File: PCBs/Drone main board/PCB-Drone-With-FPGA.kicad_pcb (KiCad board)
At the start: 4 copper layers, 60 x 100 mm, 213 parts, among them J1001 Conn_02x10, J1002 Conn_02x07, J1003 Conn_02x10, J1004 Conn_02x05, J201 PJ-102A, J601 UJ2-MBH-1-SMT-TR, J801 SMA-RP, J901 Amphenol-1mm-10-header, U1201 10CL040_F484, U301 AP63205WU-7, U401 SC189ZSKTRT, U402 NCP115ASN250T2G, U501 AP63200WU-7, U601 93LCxxBxxOT, U602 FT232H, U603 MT25QL512ABB8ESF-0SIT, U604 W25Q128JVS, U701 ICM-20602, U702 TXB0108PWR, U703 BNO055, U704 DPS422XTSA1, U705 MCP3208, U801 nRF24L01P, U802 RFX2401C, X1401 SiT2001B1-S2-33E-50, X801 16MHz, Y601 12MHz, Y701 32.7KHz

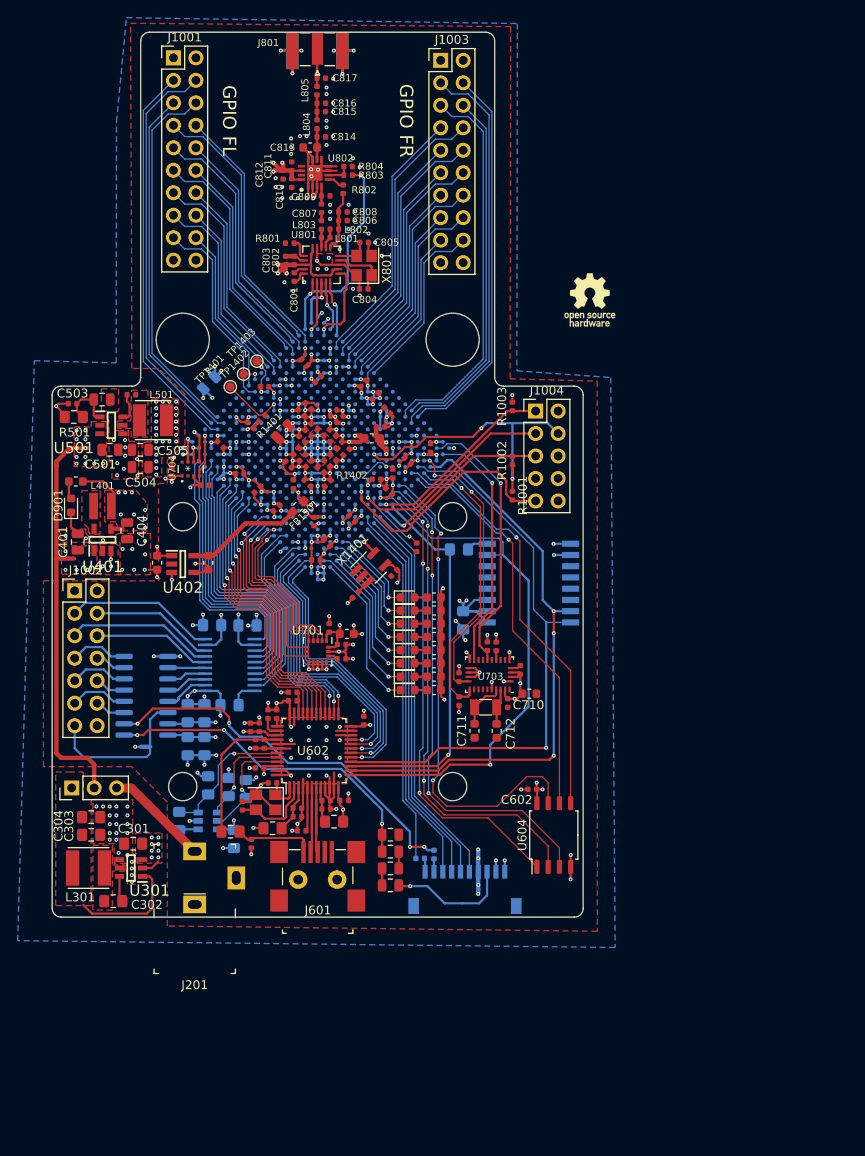
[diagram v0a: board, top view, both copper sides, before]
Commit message: Redid the radio PCB layout on both drone and remote PCB. Drone PCB had old schematic, remote PCB layout wasn't ideal.
Copied in the VHDL project files from the seperate VHDL project into the main "All in one" project.

Signed-off-by: Eldalote.Electronics <Eldalote.Electronics@gmail.com>
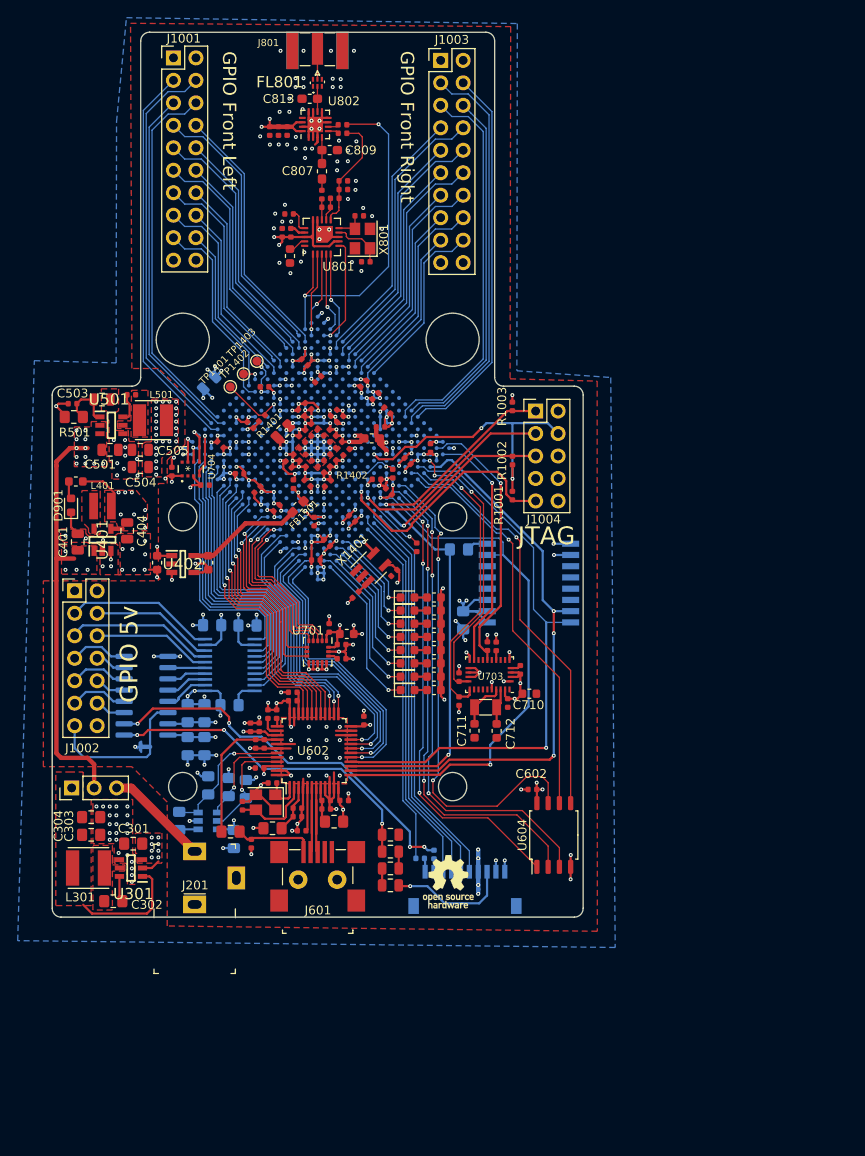
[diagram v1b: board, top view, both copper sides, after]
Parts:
- removed C814, C815, C816, C817: 1pF, Capacitor_SMD:C_0402_1005Metric
- removed L804, L805: 2.7nH, Inductor_SMD:L_0402_1005Metric
- removed R804: 2K, Resistor_SMD:R_0402_1005Metric
- added FL801: 2450LP14A100T, SamacSys_Parts:2450LP14A100T, F.Cu at (130.0, 45.7)
- C801: footprint Capacitor_SMD:C_0402_1005Metric -> Capacitor_SMD:C_0603_1608Metric
- C807, C809: footprint Capacitor_SMD:C_0402_1005Metric -> Capacitor_SMD:C_0603_1608Metric_Pad1.05x0.95mm_HandSolder
- C813: footprint Capacitor_SMD:C_0603_1608Metric -> Capacitor_SMD:C_0603_1608Metric_Pad1.05x0.95mm_HandSolder
- J801: value SMA-RP -> SMA
- U801: footprint Package_DFN_QFN:QFN-20-1EP_4x4mm_P0.5mm_EP2.5x2.5mm -> Eldalote-footprints:nRF24L01P-QFN-20-1EP_4x4mm_P0.5mm_EP
- U802: footprint SamacSys_Parts:QFN50P300X300X60-17N-D -> Package_DFN_QFN:QFN-16-1EP_3x3mm_P0.5mm_EP1.75x1.75mm
- moved LOGO101 67.7 mm to (144.8, 136.0)
- moved R802 6.33 mm to (132.8, 51.4), turned to 180 degrees
- moved C810 5.91 mm to (126.5, 51.2)
- moved R803 5.72 mm to (132.8, 50.5)
- moved C813 5.51 mm to (129.1, 47.5)
- moved U802 5.47 mm to (129.7, 50.4)
- moved C809 5.20 mm to (131.4, 53.3)
- moved C812 5.17 mm to (124.6, 51.2)
- moved C806 4.49 mm to (132.9, 56.8)
- moved C811 4.24 mm to (125.6, 51.2), turned to 90 degrees
- moved C807 4.20 mm to (130.5, 55.7)
- moved L802 3.49 mm to (131.9, 58.8)
- moved L803 3.44 mm to (130.5, 58.4)
- moved L801 3.43 mm to (131.0, 59.8)
- moved R801 3.30 mm to (126.8, 60.5)
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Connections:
- net Net-(R802-Pad2) renamed /nRF24L01+ Radio module/TXEN
- net Net-(R803-Pad2) renamed /nRF24L01+ Radio module/RXEN
- U802 pad 15: Net-(U802-Pad15) -> GND
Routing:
- net GND: track 301.1 -> 270.0 mm, vias 242 -> 244
- net nRF_CE: track 24.9 -> 39.9 mm
- net /nRF24L01+ Radio module/VDD_PA: track 6.94 -> 13.0 mm
- net nRF_MISO: track 6.39 -> 9.80 mm
- net nRF_MOSI: track 5.81 -> 9.12 mm
- net nRF_CSn: track 6.31 -> 9.48 mm
- net Net-(C815-Pad2): track 2.83 -> 0.00 mm
- net nRF_SCLK: track 5.70 -> 8.27 mm
- net nRF_IRQ: track 9.67 -> 12.2 mm
- net /nRF24L01+ Radio module/RXEN: track 2.73 -> 1.22 mm
- net Net-(C807-Pad1): track 2.02 -> 2.93 mm
- net Net-(FL801-Pad5): track 4.25 -> 3.45 mm
- net /nRF24L01+ Radio module/TXEN: track 1.95 -> 1.22 mm
- net +3V3: track 166.2 -> 165.5 mm, vias 76 -> 74
- net Net-(C801-Pad1): track 1.30 -> 2.02 mm
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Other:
- board text added: "GPIO 5v"
- board text added: "GPIO Front Left"
- board text added: "GPIO Front Right"
- board text added: "JTAG"
- board text removed: "GPIO FL"
- board text removed: "GPIO FR"

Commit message: Some cleanup, and PCB antenna removal.
Last edits before asking for reddit feedback.

Signed-off-by: Eldalote.Electronics <Eldalote.Electronics@gmail.com>
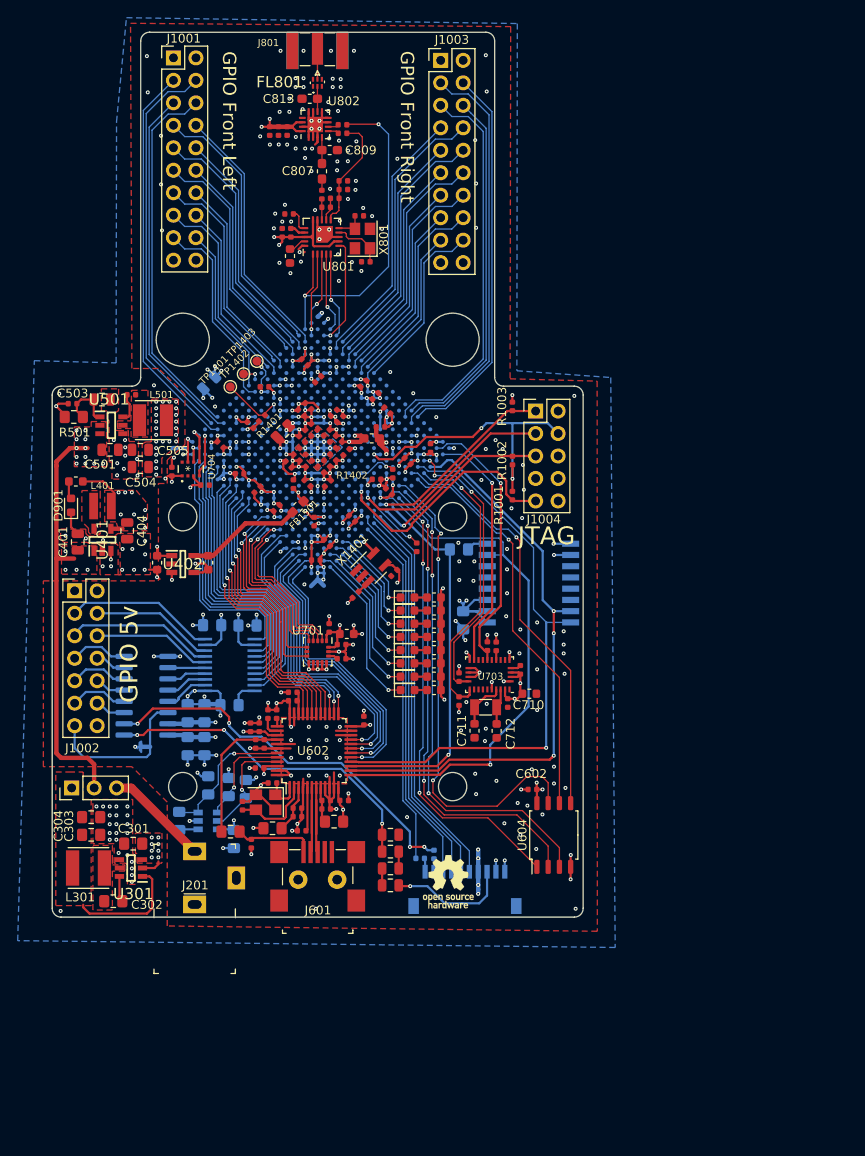
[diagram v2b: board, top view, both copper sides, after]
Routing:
- net GND: track 270.0 -> 277.0 mm, vias 244 -> 321

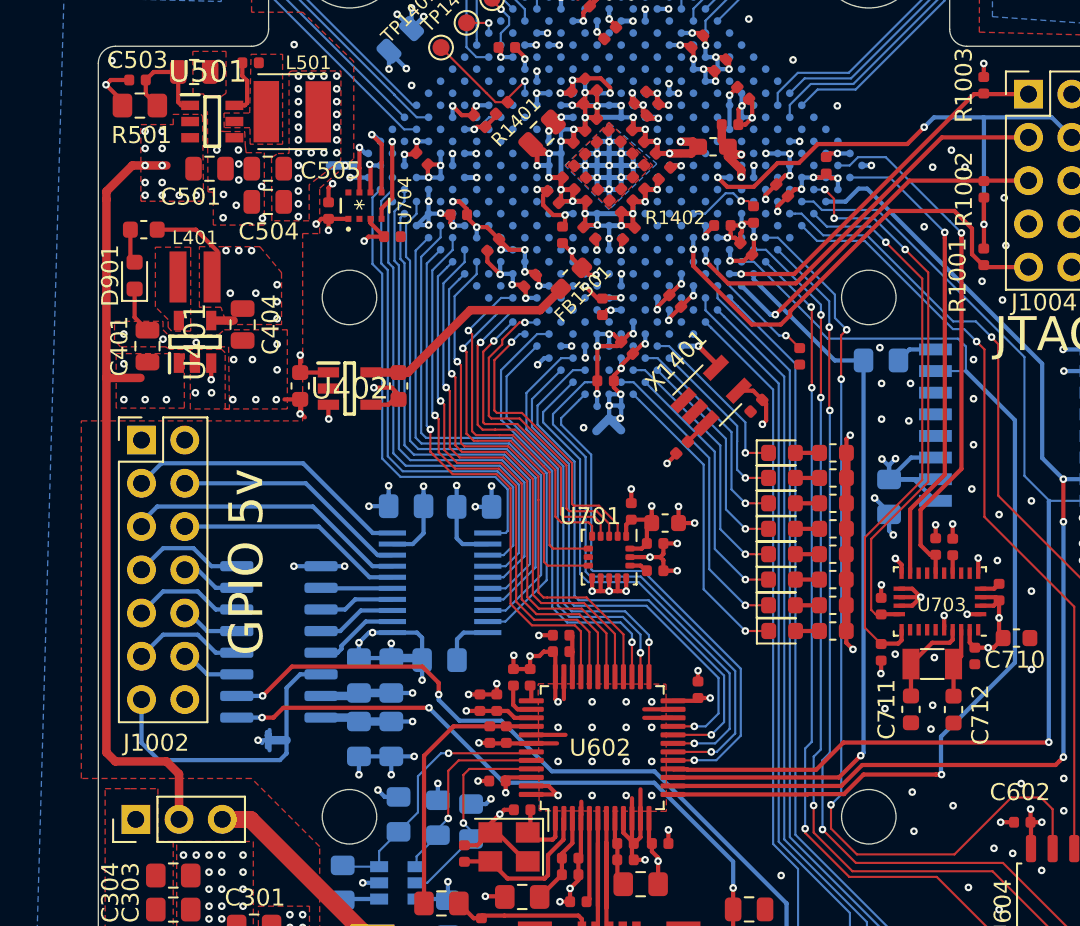
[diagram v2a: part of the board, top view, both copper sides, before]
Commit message: Minor tweaks. Improved groundplane around FPGA core (removed and relocated a few power vias) and flipped clock circuit to the same side as the FPGA.
Signed-off-by: Eldalote.Electronics <Eldalote.Electronics@gmail.com>
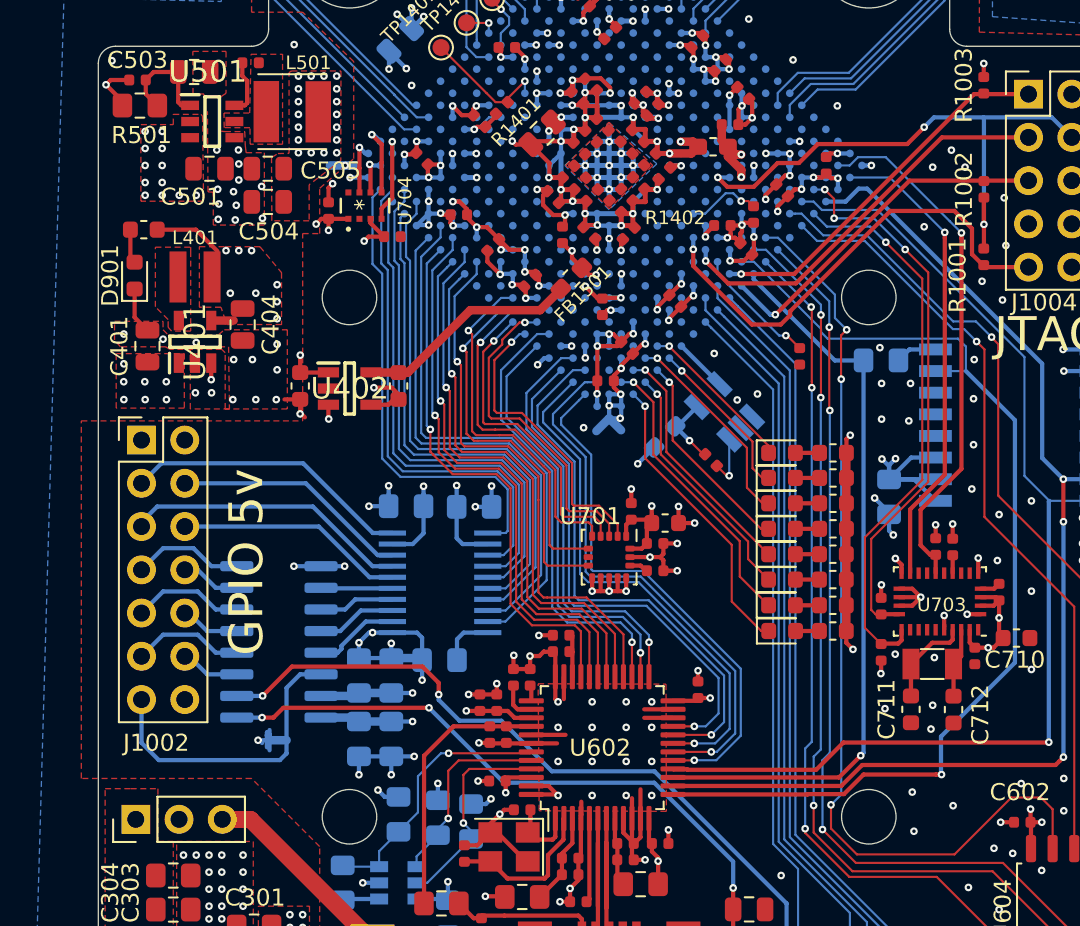
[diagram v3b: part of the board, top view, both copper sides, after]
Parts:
- C1401: footprint Inductor_SMD:L_0402_1005Metric -> Inductor_SMD:L_0603_1608Metric_Pad1.05x0.95mm_HandSolder; moved to B.Cu
- C613, C615: value 4u7F -> 4.7uF
- L301: value 4u7H 2.6ADC -> 4.7uH 2.6ADC
- X1401: value SiT2001B1-S2-33E-50 -> SiT2001BI-S2-33E-50.000000G; moved to B.Cu
- moved C1401 5.69 mm to (133.3, 102.9)
- moved R1405 1.85 mm to (136.0, 104.3), turned to 315 degrees
- moved X1401 1.24 mm to (136.8, 101.5), turned to 135 degrees
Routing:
- net +5V: track 67.7 -> 21.1 mm, vias 20 -> 23
- net Net-(R1405-Pad2): track 1.54 -> 3.09 mm, vias 0 -> 1
- net GND: track 277.0 -> 278.4 mm, vias 321 -> 328
- net USERLED1: track 17.9 -> 17.1 mm
- net USERLED2: track 15.4 -> 14.6 mm
- net USERLED7: track 10.2 -> 9.39 mm
- net USERLED3: track 15.3 -> 14.5 mm
- net USERLED5: track 12.7 -> 12.1 mm
- net USERLED6: track 10.3 -> 9.67 mm
- net USERLED0: track 18.0 -> 17.5 mm
- net USERLED4: track 12.8 -> 12.3 mm
- net /FPGA Part 3/FPGA-CLOCK-50: track 2.71 -> 3.17 mm, vias 1 -> 0
- net +1V2: track 84.3 -> 84.7 mm, vias 52 -> 43
- net +3V3: track 165.5 -> 165.6 mm, vias 74 -> 73

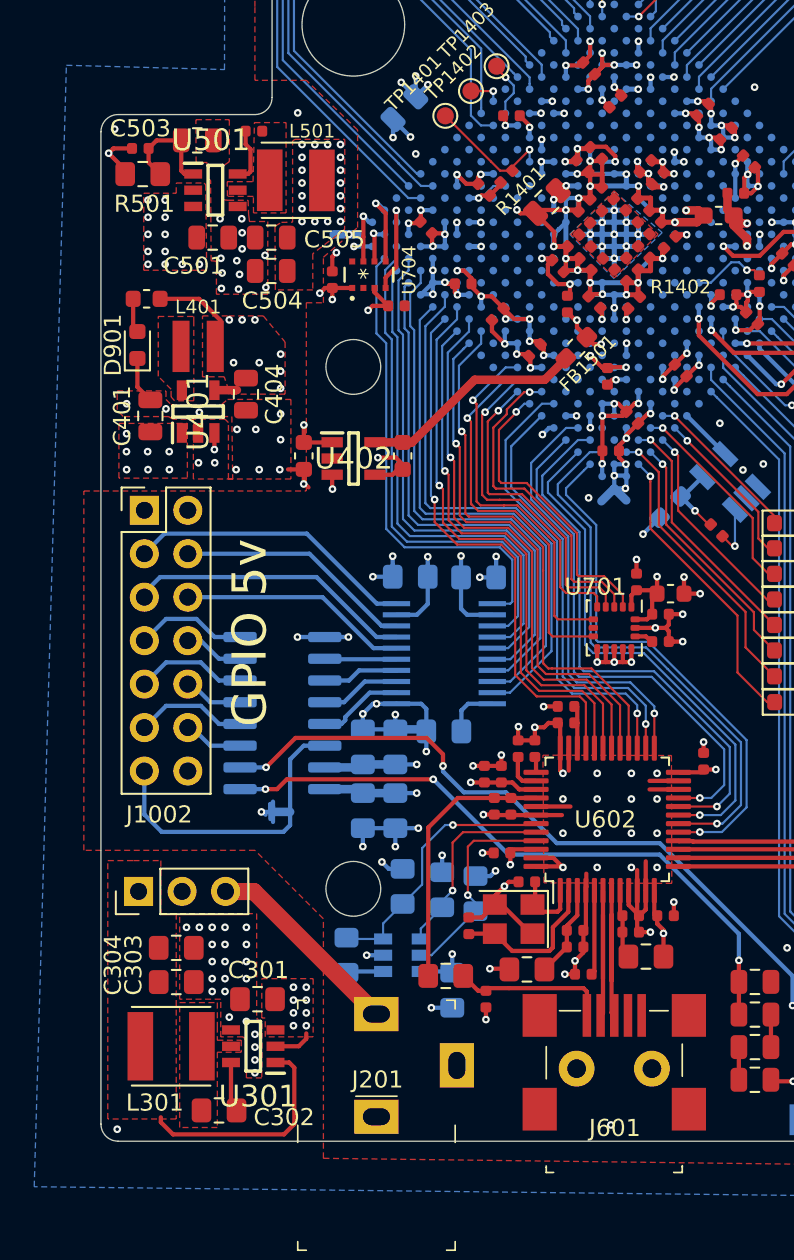
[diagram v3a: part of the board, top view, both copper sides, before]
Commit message: Lots of work to check every component, add Manufacturers number (instead of LCSC or digikey and mouser numbers)
Changed to USB-C connector, almost done with that sheet. Components checked, need to redo Sheet IO

Signed-off-by: Eldalote.Electronics <Eldalote.Electronics@gmail.com>
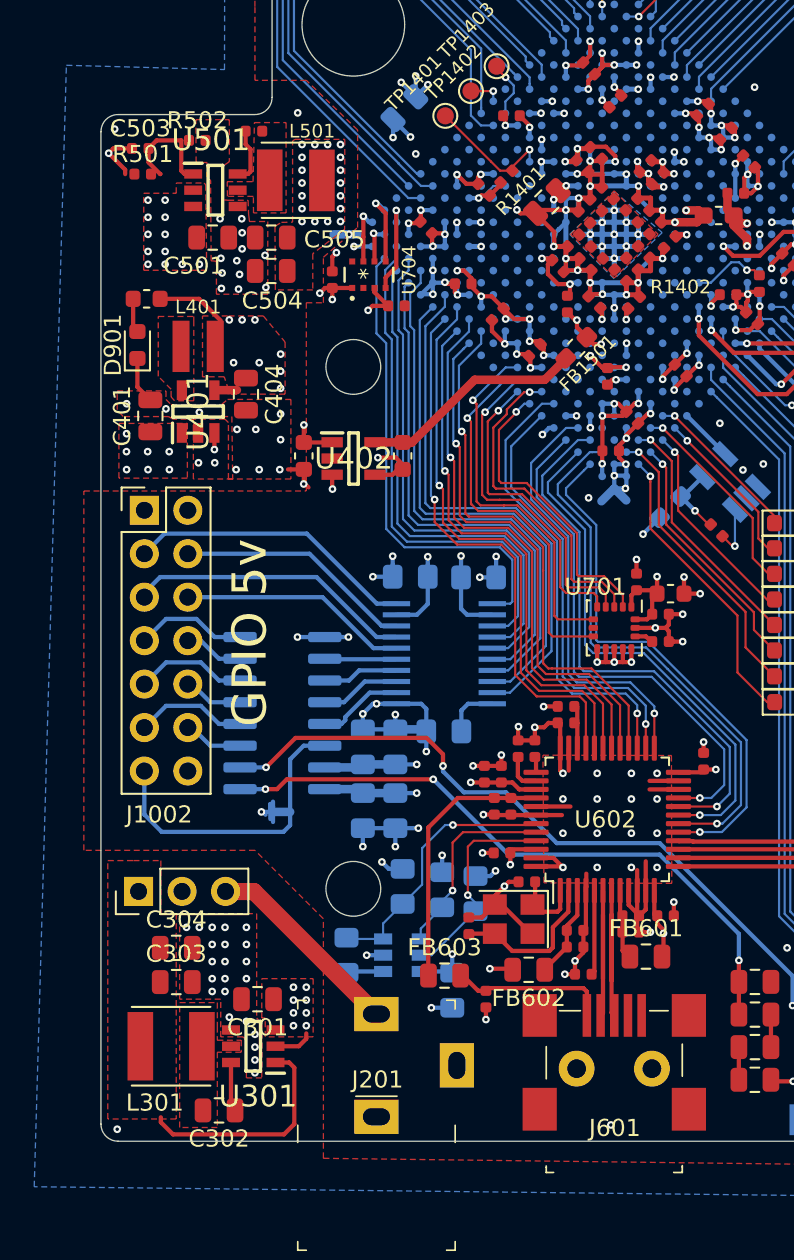
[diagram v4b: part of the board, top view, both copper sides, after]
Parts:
- C1509, C1510, C1511, C1512, C1513, C1514, C1515, C1516, C1519, C1526, C1532, C1538, C604, C605: value 4u7F -> 4.7uF
- C301, C302, C303, C304: footprint Capacitor_SMD:C_0805_2012Metric_Pad1.15x1.40mm_HandSolder -> Capacitor_SMD:C_0805_2012Metric
- C702: value 2u2F -> 2.2uF
- C710: value 4n7F -> 4.7nF
- FB601, FB602, FB603: footprint Resistor_SMD:R_0805_2012Metric_Pad1.15x1.40mm_HandSolder -> Resistor_SMD:R_0805_2012Metric
- L501: value 2u2H -> 2.2uH
- R501: footprint Resistor_SMD:R_0805_2012Metric_Pad1.15x1.40mm_HandSolder -> Resistor_SMD:R_0402_1005Metric
- R502: footprint Resistor_SMD:R_0805_2012Metric -> Resistor_SMD:R_0402_1005Metric
- moved FB602 0.10 mm to (125.0, 130.0)
- moved FB603 0.07 mm to (120.1, 130.3)
